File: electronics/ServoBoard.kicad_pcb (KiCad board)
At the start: 2 copper layers, 64 x 56 mm, 13 parts, among them K1 Left Servo, K2 Right Servo, P1 Pi GPIO Header, P2 CONN_2, P3 CONNECTOR, P4 CONNECTOR, P5 CONNECTOR, P6 CONNECTOR, P7 CONN_2, U1 7805

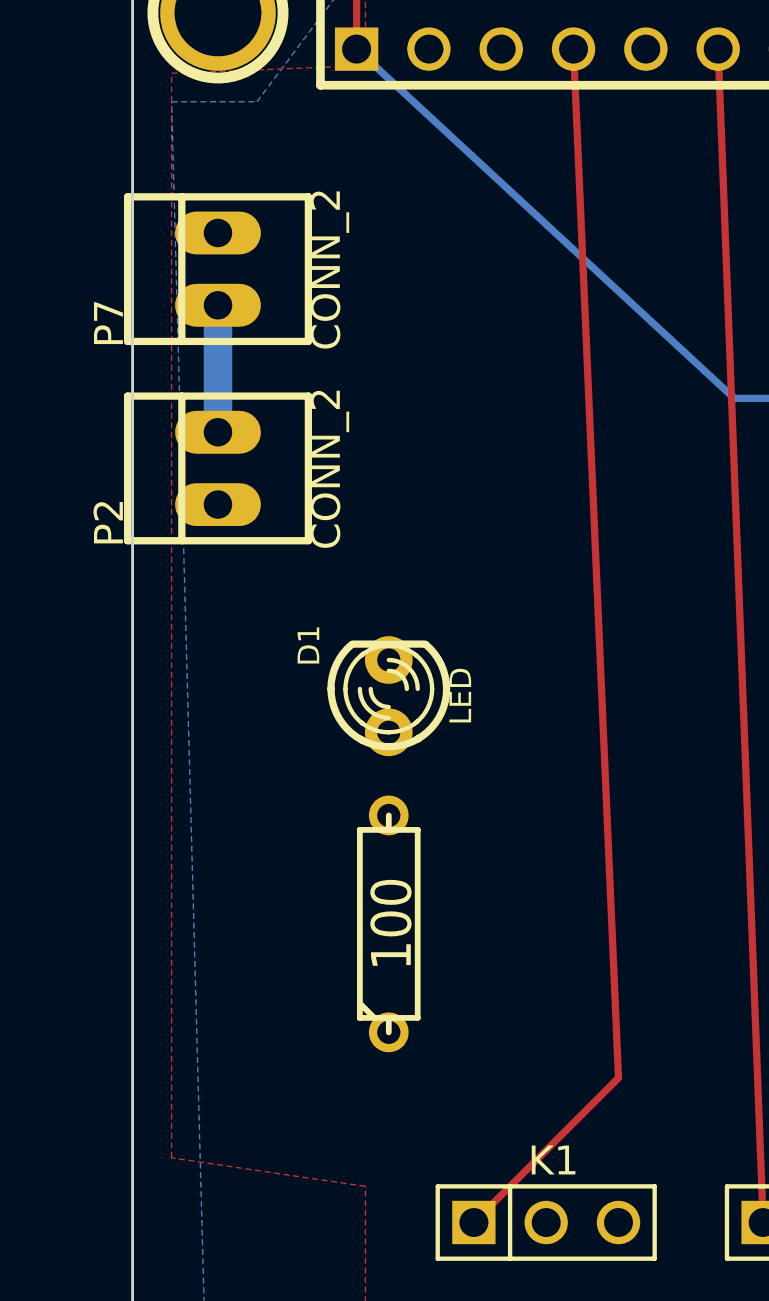
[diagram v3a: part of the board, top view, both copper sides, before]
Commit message: Updated to use screw terminals
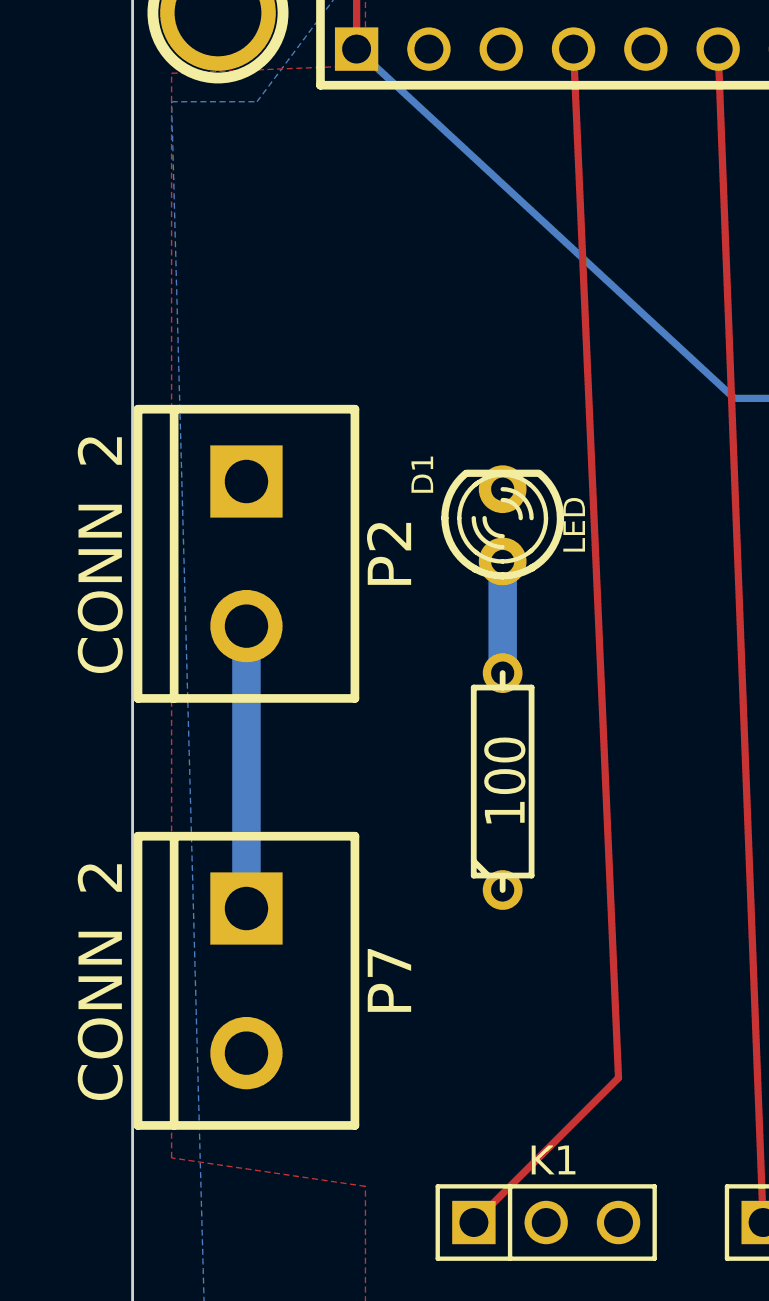
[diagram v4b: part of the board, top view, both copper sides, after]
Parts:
- P2, P7: footprint PINHEAD1-2 -> bornier2
- moved P7 25.0 mm to (130.0, 105.0), turned to 270 degrees
- moved D1 7.21 mm to (139.0, 89.0)
- moved R1 6.40 mm to (139.0, 98.0)
- moved P2 3.16 mm to (130.0, 90.0), turned to 270 degrees
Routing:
- net N-0000031: track 4.46 -> 9.92 mm
- net N-0000027: track 0.00 -> 3.92 mm
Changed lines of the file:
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@@
   (general
     (links 17)
-    (no_connects 1)
+    (no_connects 0)
     (area 125.949999 67.949999 190.050001 124.050001)
     (thickness 1.6)
     (drawings 18)
-    (tracks 7)
+    (tracks 8)
     (zones 0)
     (modules 13)
@@
   )
   (module R3 (layer F.Cu)
-    (at 135 103 90)
+    (at 139 98 90)
     (descr "Resitance 3 pas")
     (tags R)
@@
   )
   (module LED-3MM (layer F.Cu)
-    (at 135 95 90)
+    (at 139 89 90)
     (descr "LED 3mm - Lead pitch 100mil (2,54mm)")
     (tags "LED led 3mm 3MM 100mil 2,54mm")
@@
     )
   )
-  (module PINHEAD1-2 (layer F.Cu)
-    (at 129 87 90)
-    (attr virtual)
-    (fp_text reference P2 (at -1.905 -3.81 90) (layer F.SilkS)
-      (effects (font (size 1.016 1.016) (thickness 0.0889)))
-    )
-    (fp_text value CONN_2 (at 0 3.81 90) (layer F.SilkS)
-      (effects (font (size 1.016 1.016) (thickness 0.0889)))
-    )
-    (fp_line (start 2.54 -1.27) (end -2.54 -1.27) (layer F.SilkS) (width 0.254))
-    (fp_line (start 2.54 3.175) (end -2.54 3.175) (layer F.SilkS) (width 0.254))
-    (fp_line (start -2.54 -3.175) (end 2.54 -3.175) (layer F.SilkS) (width 0.254))
-    (fp_line (start -2.54 -3.175) (end -2.54 3.175) (layer F.SilkS) (width 0.254))
-    (fp_line (start 2.54 -3.175) (end 2.54 3.175) (layer F.SilkS) (width 0.254))
-    (pad 1 thru_hole oval (at -1.27 0 90) (size 1.50622 3.01498) (drill 0.99822)
-      (layers *.Cu F.Paste F.SilkS F.Mask)
-      (net 2 GND)
-    )
-    (pad 2 thru_hole oval (at 1.27 0 90) (size 1.50622 3.01498) (drill 0.99822)
-      (layers *.Cu F.Paste F.SilkS F.Mask)
-      (net 5 N-0000031)
-    )
-  )
   (module 1pin (layer F.Cu)
     (at 187 71)
@@
     )
   )
-  (module PINHEAD1-2 (layer F.Cu)
-    (at 129 80 90)
-    (attr virtual)
-    (fp_text reference P7 (at -1.905 -3.81 90) (layer F.SilkS)
-      (effects (font (size 1.016 1.016) (thickness 0.0889)))
-    )
-    (fp_text value CONN_2 (at 0 3.81 90) (layer F.SilkS)
-      (effects (font (size 1.016 1.016) (thickness 0.0889)))
-    )
-    (fp_line (start 2.54 -1.27) (end -2.54 -1.27) (layer F.SilkS) (width 0.254))
-    (fp_line (start 2.54 3.175) (end -2.54 3.175) (layer F.SilkS) (width 0.254))
-    (fp_line (start -2.54 -3.175) (end 2.54 -3.175) (layer F.SilkS) (width 0.254))
-    (fp_line (start -2.54 -3.175) (end -2.54 3.175) (layer F.SilkS) (width 0.254))
-    (fp_line (start 2.54 -3.175) (end 2.54 3.175) (layer F.SilkS) (width 0.254))
-    (pad 1 thru_hole oval (at -1.27 0 90) (size 1.50622 3.01498) (drill 0.99822)
-      (layers *.Cu F.Paste F.SilkS F.Mask)
+  (module bornier2 (layer F.Cu)
+    (at 130 90 270)
+    (descr "Bornier d'alimentation 2 pins")
+    (tags DEV)
+    (fp_text reference P2 (at 0 -5.08 270) (layer F.SilkS)
+      (effects (font (size 1.524 1.524) (thickness 0.3048)))
+    )
+    (fp_text value CONN_2 (at 0 5.08 270) (layer F.SilkS)
+      (effects (font (size 1.524 1.524) (thickness 0.3048)))
+    )
+    (fp_line (start 5.08 2.54) (end -5.08 2.54) (layer F.SilkS) (width 0.3048))
+    (fp_line (start 5.08 3.81) (end 5.08 -3.81) (layer F.SilkS) (width 0.3048))
+    (fp_line (start 5.08 -3.81) (end -5.08 -3.81) (layer F.SilkS) (width 0.3048))
+    (fp_line (start -5.08 -3.81) (end -5.08 3.81) (layer F.SilkS) (width 0.3048))
+    (fp_line (start -5.08 3.81) (end 5.08 3.81) (layer F.SilkS) (width 0.3048))
+    (pad 1 thru_hole rect (at -2.54 0 270) (size 2.54 2.54) (drill 1.524)
+      (layers *.Cu *.Mask F.SilkS)
+      (net 2 GND)
+    )
+    (pad 2 thru_hole circle (at 2.54 0 270) (size 2.54 2.54) (drill 1.524)
+      (layers *.Cu *.Mask F.SilkS)
       (net 5 N-0000031)
     )
-    (pad 2 thru_hole oval (at 1.27 0 90) (size 1.50622 3.01498) (drill 0.99822)
-      (layers *.Cu F.Paste F.SilkS F.Mask)
+    (model device/bornier_2.wrl
+      (at (xyz 0 0 0))
+      (scale (xyz 1 1 1))
+      (rotate (xyz 0 0 0))
+    )
+  )
+  (module bornier2 (layer F.Cu)
+    (at 130 105 270)
+    (descr "Bornier d'alimentation 2 pins")
+    (tags DEV)
+    (fp_text reference P7 (at 0 -5.08 270) (layer F.SilkS)
+      (effects (font (size 1.524 1.524) (thickness 0.3048)))
+    )
+    (fp_text value CONN_2 (at 0 5.08 270) (layer F.SilkS)
+      (effects (font (size 1.524 1.524) (thickness 0.3048)))
+    )
+    (fp_line (start 5.08 2.54) (end -5.08 2.54) (layer F.SilkS) (width 0.3048))
+    (fp_line (start 5.08 3.81) (end 5.08 -3.81) (layer F.SilkS) (width 0.3048))
+    (fp_line (start 5.08 -3.81) (end -5.08 -3.81) (layer F.SilkS) (width 0.3048))
+    (fp_line (start -5.08 -3.81) (end -5.08 3.81) (layer F.SilkS) (width 0.3048))
+    (fp_line (start -5.08 3.81) (end 5.08 3.81) (layer F.SilkS) (width 0.3048))
+    (pad 1 thru_hole rect (at -2.54 0 270) (size 2.54 2.54) (drill 1.524)
+      (layers *.Cu *.Mask F.SilkS)
+      (net 5 N-0000031)
+    )
+    (pad 2 thru_hole circle (at 2.54 0 270) (size 2.54 2.54) (drill 1.524)
+      (layers *.Cu *.Mask F.SilkS)
       (net 1 +6V)
+    )
+    (model device/bornier_2.wrl
+      (at (xyz 0 0 0))
+      (scale (xyz 1 1 1))
+      (rotate (xyz 0 0 0))
     )
   )
@@
   (segment (start 141.49 72.27) (end 143.07 108.41) (width 0.254) (layer F.Cu) (net 3) (status 10))
   (segment (start 143.07 108.41) (end 137.99 113.49) (width 0.254) (layer F.Cu) (net 3))
-  (segment (start 129 81.27) (end 129 85.73) (width 1) (layer B.Cu) (net 5) (status C00000))
+  (segment (start 139 90.27) (end 139 94.19) (width 1) (layer B.Cu) (net 4))
+  (segment (start 130 92.54) (end 130 102.46) (width 1) (layer B.Cu) (net 5))
   (segment (start 163 84.54) (end 147.14 84.54) (width 0.254) (layer B.Cu) (net 6))
   (segment (start 147.14 84.54) (end 133.87 72.27) (width 0.254) (layer B.Cu) (net 6) (status 20))
